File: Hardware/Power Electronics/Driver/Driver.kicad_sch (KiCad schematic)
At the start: 3 parts, among them J1 Conn_01x28, J2 Conn_01x28, U1 DRV8301DCAR

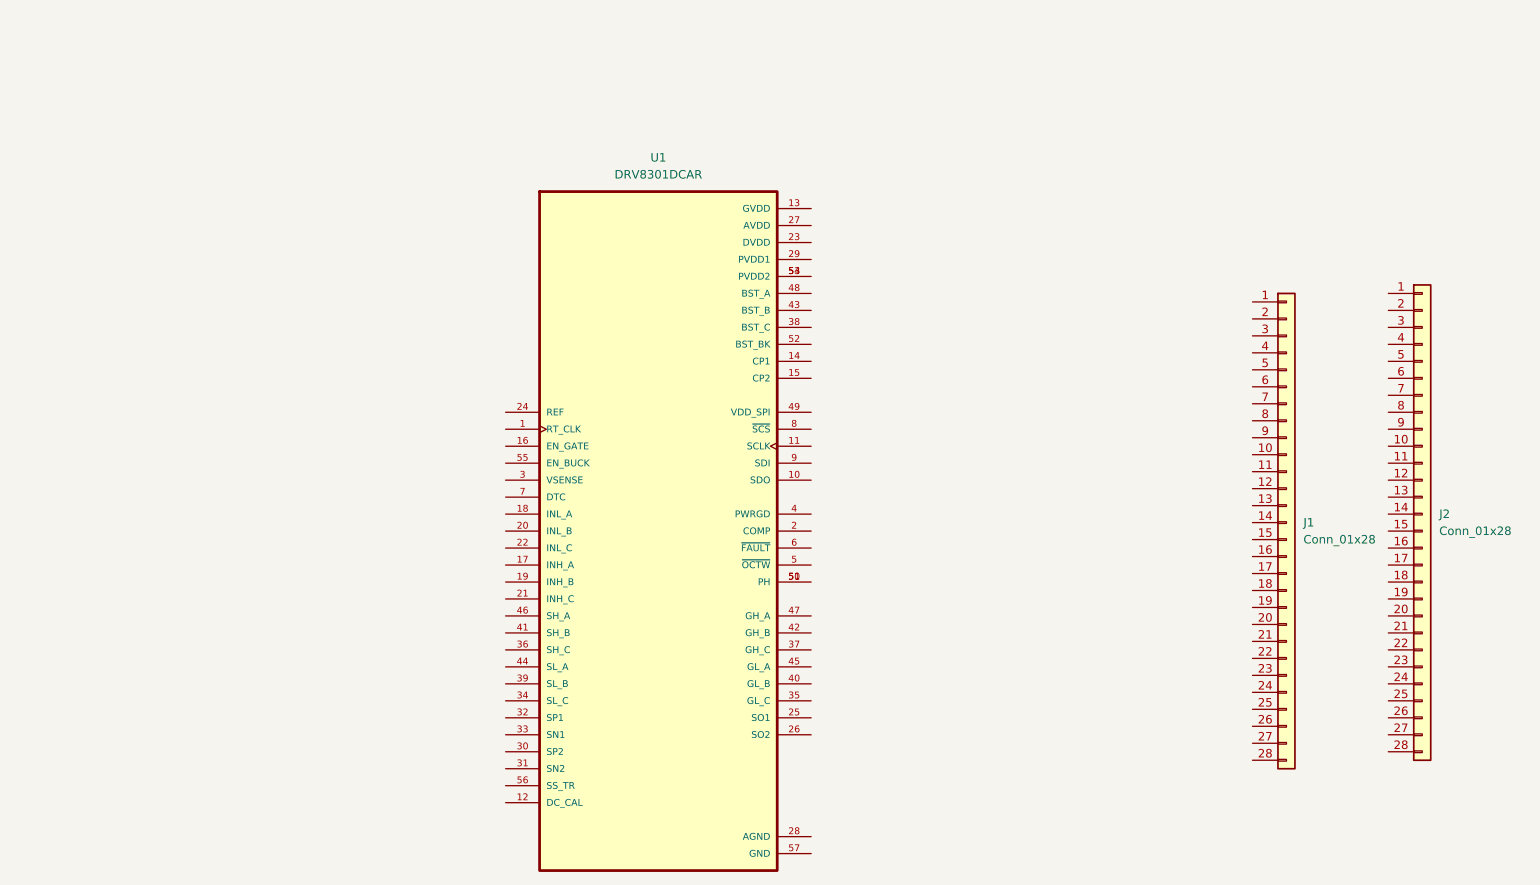
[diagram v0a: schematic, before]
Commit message: fix: drv footprint correction
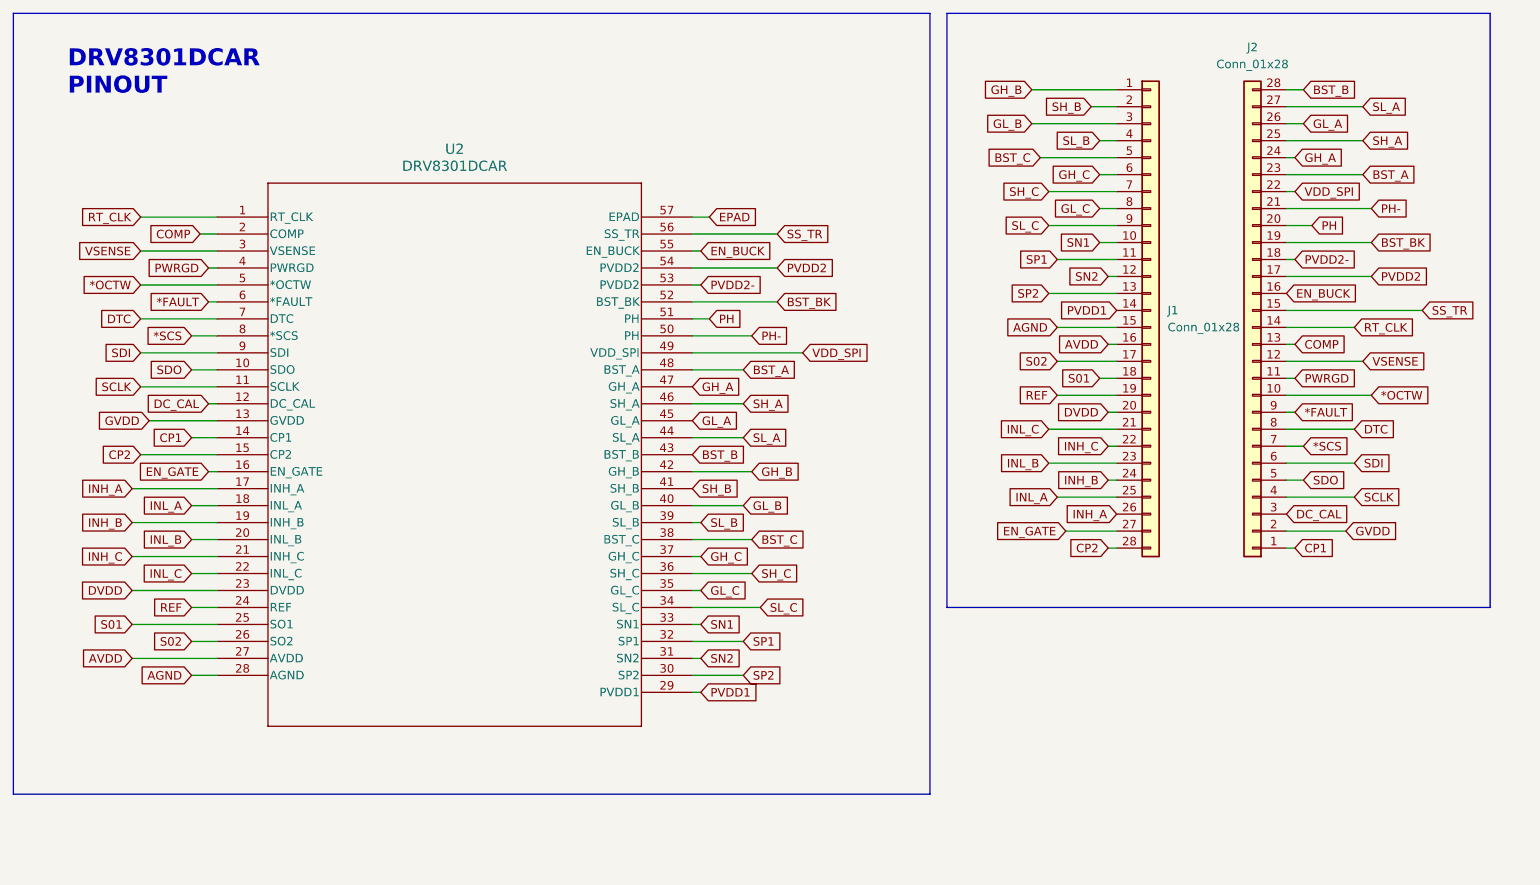
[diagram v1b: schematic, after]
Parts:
- removed U1: DRV8301DCAR, DRV8301DCAR:SOP50P810X120-57N, symbol drv8301car:DRV8301DCAR
- added U2: DRV8301DCAR, DRV8301DCAR:DRV8301DCAR PADGND, symbol DRV8301DCAR:DRV8301DCAR
- J1, J2: footprint (none) -> Connector_PinHeader_2.54mm:PinHeader_1x28_P2.54mm_Vertical
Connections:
- net GH_B: now reaches J1.1 (Pin_1)
- net GH_B: now also U2.42 (GH_B)
- net SN1: now reaches J1.10 (Pin_10)
- net SN1: now also U2.33 (SN1)
- net SP1: now reaches J1.11 (Pin_11)
- net SP1: now also U2.32 (SP1)
- net SN2: now reaches J1.12 (Pin_12)
- net SN2: now also U2.31 (SN2)
- net SP2: now reaches J1.13 (Pin_13)
- net SP2: now also U2.30 (SP2)
- net PVDD1: now reaches J1.14 (Pin_14)
- net PVDD1: now also U2.29 (PVDD1)
- net AGND: now reaches J1.15 (Pin_15)
- net AGND: now also U2.28 (AGND)
- net AVDD: now reaches J1.16 (Pin_16)
- net AVDD: now also U2.27 (AVDD)
- net S02: now reaches J1.17 (Pin_17)
- net S02: now also U2.26 (SO2)
- net S01: now reaches J1.18 (Pin_18)
- net S01: now also U2.25 (SO1)
- net REF: now reaches J1.19 (Pin_19)
- net REF: now also U2.24 (REF)
- net SH_B: now reaches J1.2 (Pin_2)
- net SH_B: now also U2.41 (SH_B)
- net DVDD: now reaches J1.20 (Pin_20)
- net DVDD: now also U2.23 (DVDD)
- net INL_C: now reaches J1.21 (Pin_21)
- net INL_C: now also U2.22 (INL_C)
- net INH_C: now reaches J1.22 (Pin_22)
- net INH_C: now also U2.21 (INH_C)
- net INL_B: now reaches J1.23 (Pin_23)
- net INL_B: now also U2.20 (INL_B)
- net INH_B: now reaches J1.24 (Pin_24)
- net INH_B: now also U2.19 (INH_B)
- net INL_A: now reaches J1.25 (Pin_25)
- net INL_A: now also U2.18 (INL_A)
- net INH_A: now reaches J1.26 (Pin_26)
- net INH_A: now also U2.17 (INH_A)
- net EN_GATE: now reaches J1.27 (Pin_27)
- net EN_GATE: now also U2.16 (EN_GATE)
- net CP2: now reaches J1.28 (Pin_28)
- net CP2: now also U2.15 (CP2)
- net GL_B: now reaches J1.3 (Pin_3)
- net GL_B: now also U2.40 (GL_B)
- net SL_B: now reaches J1.4 (Pin_4)
- net SL_B: now also U2.39 (SL_B)
- net BST_C: now reaches J1.5 (Pin_5)
- net BST_C: now also U2.38 (BST_C)
- net GH_C: now reaches J1.6 (Pin_6)
- net GH_C: now also U2.37 (GH_C)
- net SH_C: now reaches J1.7 (Pin_7)
- net SH_C: now also U2.36 (SH_C)
- net GL_C: now reaches J1.8 (Pin_8)
- net GL_C: now also U2.35 (GL_C)
- net SL_C: now reaches J1.9 (Pin_9)
- net SL_C: now also U2.34 (SL_C)
- net CP1: now reaches J2.1 (Pin_1)
- net CP1: now also U2.14 (CP1)
- net *OCTW: now reaches J2.10 (Pin_10)
- net *OCTW: now also U2.5 (*OCTW)
- net PWRGD: now reaches J2.11 (Pin_11)
- net PWRGD: now also U2.4 (PWRGD)
- net VSENSE: now reaches J2.12 (Pin_12)
- net VSENSE: now also U2.3 (VSENSE)
- net COMP: now reaches J2.13 (Pin_13)
- net COMP: now also U2.2 (COMP)
- net RT_CLK: now reaches J2.14 (Pin_14)
- net RT_CLK: now also U2.1 (RT_CLK)
- net SS_TR: now reaches J2.15 (Pin_15)
- net SS_TR: now also U2.56 (SS_TR)
- net EN_BUCK: now reaches J2.16 (Pin_16)
- net EN_BUCK: now also U2.55 (EN_BUCK)
- net PVDD2: now reaches J2.17 (Pin_17)
- net PVDD2: now also U2.54 (PVDD2)
- net PVDD2-: now reaches J2.18 (Pin_18)
- net PVDD2-: now also U2.53 (PVDD2)
- net BST_BK: now reaches J2.19 (Pin_19)
- net BST_BK: now also U2.52 (BST_BK)
- net GVDD: now reaches J2.2 (Pin_2)
- net GVDD: now also U2.13 (GVDD)
- net PH: now reaches J2.20 (Pin_20)
- net PH: now also U2.51 (PH)
- net PH-: now reaches J2.21 (Pin_21)
- net PH-: now also U2.50 (PH)
- net VDD_SPI: now reaches J2.22 (Pin_22)
- net VDD_SPI: now also U2.49 (VDD_SPI)
- net BST_A: now reaches J2.23 (Pin_23)
- net BST_A: now also U2.48 (BST_A)
- net GH_A: now reaches J2.24 (Pin_24)
- net GH_A: now also U2.47 (GH_A)
- net SH_A: now reaches J2.25 (Pin_25)
- net SH_A: now also U2.46 (SH_A)
- net GL_A: now reaches J2.26 (Pin_26)
- net GL_A: now also U2.45 (GL_A)
- net SL_A: now reaches J2.27 (Pin_27)
- net SL_A: now also U2.44 (SL_A)
- net BST_B: now reaches J2.28 (Pin_28)
- net BST_B: now also U2.43 (BST_B)
- net DC_CAL: now reaches J2.3 (Pin_3)
- net DC_CAL: now also U2.12 (DC_CAL)
- net SCLK: now reaches J2.4 (Pin_4)
- net SCLK: now also U2.11 (SCLK)
- net SDO: now reaches J2.5 (Pin_5)
- net SDO: now also U2.10 (SDO)
- net SDI: now reaches J2.6 (Pin_6)
- net SDI: now also U2.9 (SDI)
- net *SCS: now reaches J2.7 (Pin_7)
- net *SCS: now also U2.8 (*SCS)
- net DTC: now reaches J2.8 (Pin_8)
- net DTC: now also U2.7 (DTC)
- net *FAULT: now reaches J2.9 (Pin_9)
- net *FAULT: now also U2.6 (*FAULT)
- new net EPAD: U2.57 (EPAD)
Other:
- note added: "DRV8301DCAR PINOUT"
- moved on the sheet: J1, J2
